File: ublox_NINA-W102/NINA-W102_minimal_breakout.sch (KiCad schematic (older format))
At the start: 15 parts, among them J1 Conn_01x15, J2 Conn_01x15, J3 6_PIN_SERIAL_TARGETLOCK, SW1 BOOT, SW2 RESET, U1 NINA-W102

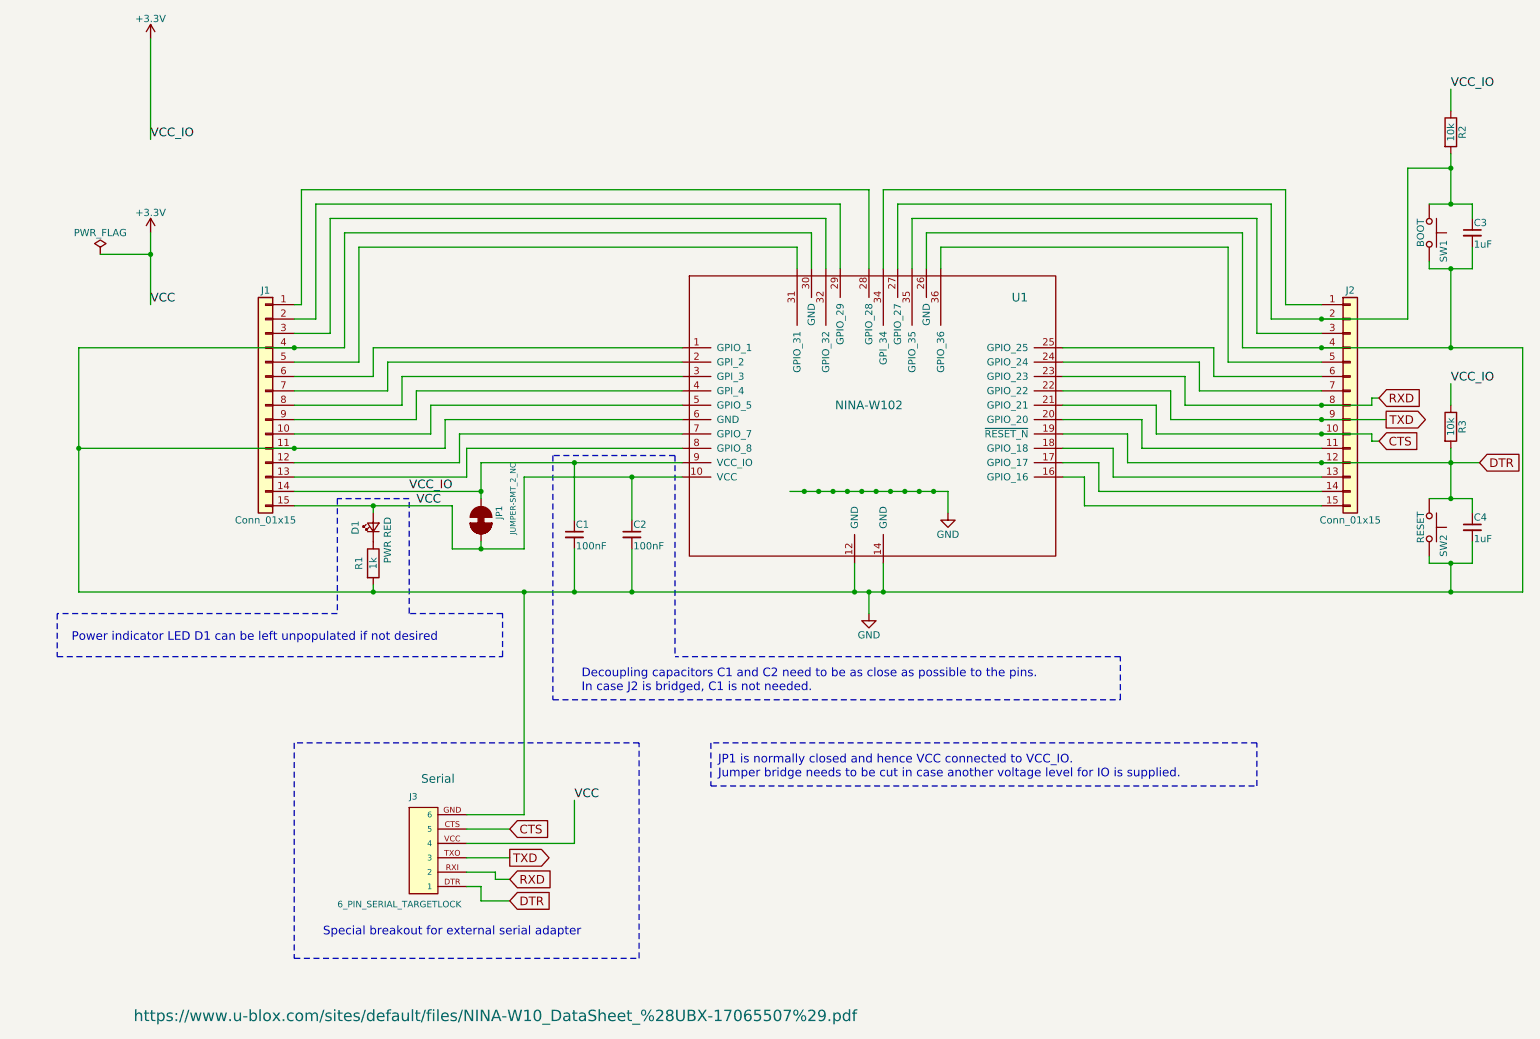
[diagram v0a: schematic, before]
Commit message: Fixed CTS PIN and added fpx sample mage from sensirion
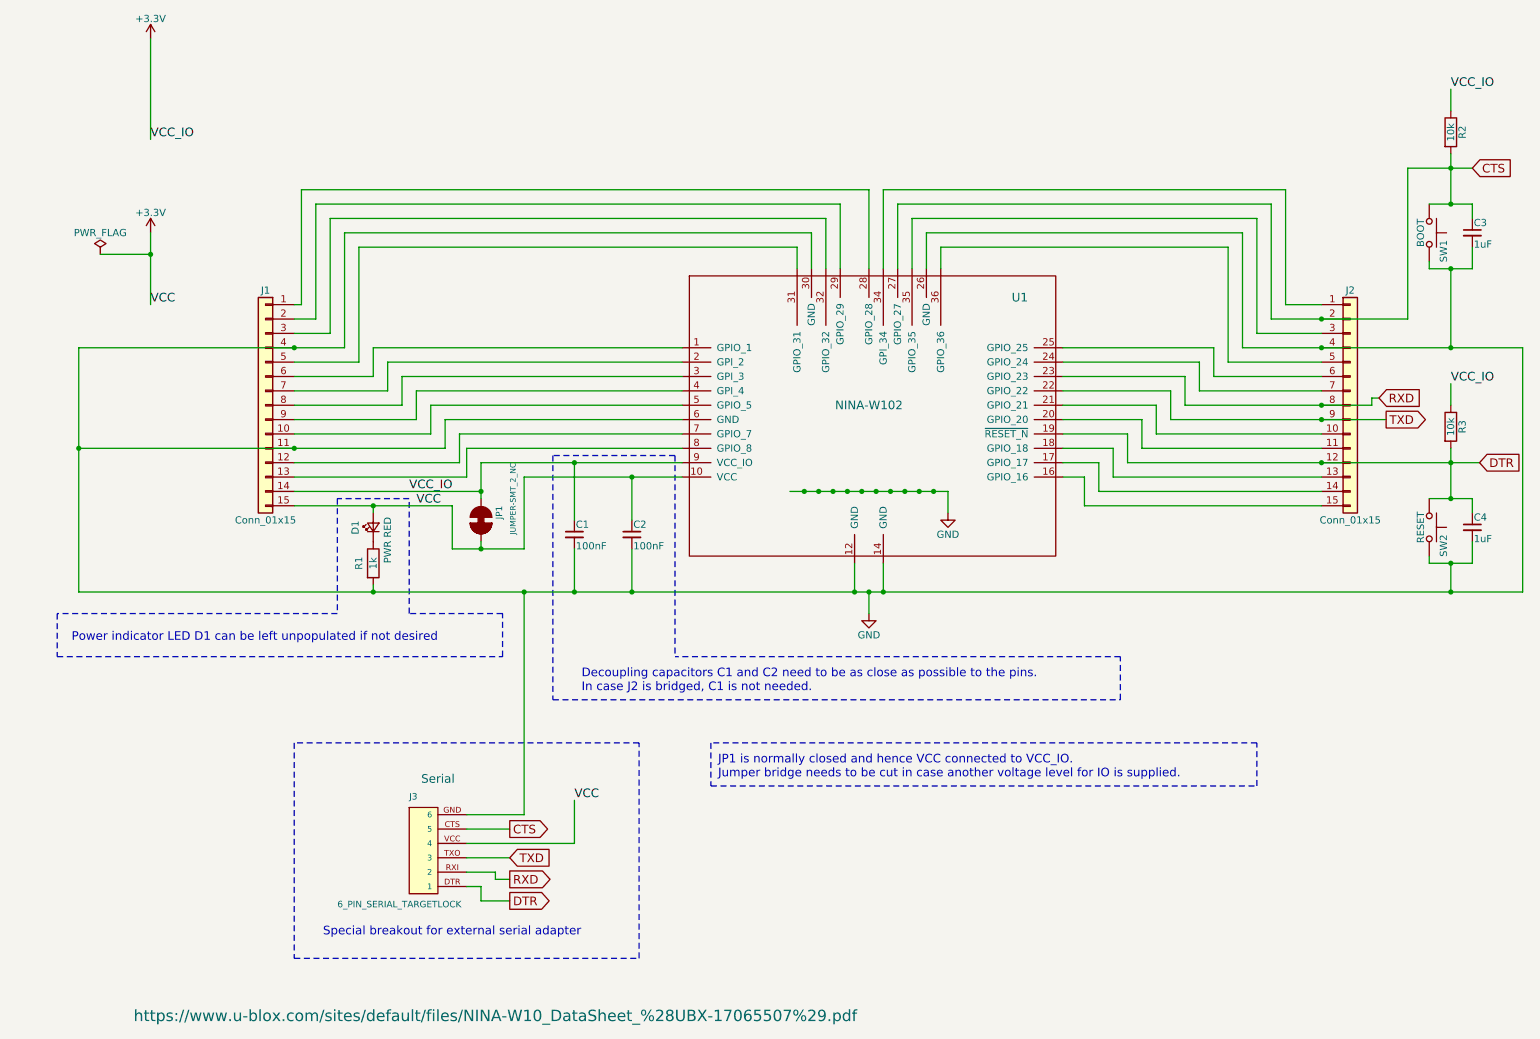
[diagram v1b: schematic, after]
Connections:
- net CTS: now also C3.1, J2.2 (Pin_2), R2.2, SW1.1, U1.27 (GPIO_27); no longer J2.10 (Pin_10), U1.21 (GPIO_21)
- new net: J2.10 (Pin_10), U1.21 (GPIO_21)
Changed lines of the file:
@@
 Sheet 1 1
 Title "ublox NINA-W102 minimal breakout"
-Date "2018-04-17"
-Rev "0.3"
+Date "2018-04-18"
+Rev "0.4"
 Comp "GDG Zürich"
 Comment1 "Michel Racic"
@@
 Text GLabel 9950 3300 2    60   Input ~ 0
 RXD
-Text GLabel 3900 6650 2    60   Input ~ 0
+Text GLabel 3900 6650 2    60   Output ~ 0
 RXD
-Text GLabel 3900 6500 2    60   Output ~ 0
+Text GLabel 3900 6500 2    60   Input ~ 0
 TXD
-Text GLabel 3900 6800 2    60   Input ~ 0
+Text GLabel 3900 6800 2    60   Output ~ 0
 DTR
-Text GLabel 3900 6300 2    60   Input ~ 0
+Text GLabel 3900 6300 2    60   Output ~ 0
 CTS
 Text GLabel 10650 3750 2    60   Input ~ 0
@@
 Text GLabel 10000 3450 2    60   Output ~ 0
 TXD
-Text GLabel 9950 3600 2    60   Input ~ 0
+Text GLabel 10600 1700 2    60   Input ~ 0
 CTS
 Text Notes 2600 7050 0    60   ~ 0
@@
 Wire Wire Line
 	8300 3450 7750 3450
-Wire Wire Line
-	8400 3550 9900 3550
 Wire Wire Line
 	8400 3550 8400 3350
@@
 	10150 2750 10150 1700
 Wire Wire Line
-	10150 1700 10450 1700
+	10150 1700 10600 1700
 Connection ~ 9550 2750
 Wire Wire Line
@@
 Connection ~ 9550 3350
 Connection ~ 9550 3450
-Connection ~ 9550 3550
 Wire Notes Line
 	2400 5700 2400 7200
@@
 Wire Wire Line
 	9900 3300 9900 3350
-Wire Wire Line
-	9950 3600 9900 3600
-Wire Wire Line
-	9900 3600 9900 3550
 Wire Wire Line
 	3700 4300 3700 4350
@@
 	1    0    0    -1
 $EndComp
+Wire Wire Line
+	2400 4050 3500 4050
+Text Label 10450 3200 0    60   ~ 0
+VCC_IO
+Text Label 3200 3950 0    60   ~ 0
+VCC_IO
+Wire Wire Line
+	8200 3750 10650 3750
+Wire Wire Line
+	2400 3950 3700 3950
+Text Label 3250 4050 0    60   ~ 0
+VCC
+Wire Wire Line
+	1400 2300 1050 2300
+Text Label 1400 2650 0    60   ~ 0
+VCC
+Text Label 10450 1150 0    60   ~ 0
+VCC_IO
+Text Label 4350 6100 0    60   ~ 0
+VCC
+Connection ~ 2400 2950
+Wire Wire Line
+	9550 3550 8400 3550
+Text Label 1400 1500 0    60   ~ 0
+VCC_IO
+Wire Wire Line
+	1400 800  1400 1500
 $Comp
 L +3.3V #PWR_IO05
@@
 	1    0    0    -1
 $EndComp
-Wire Wire Line
-	1400 800  1400 1500
-Wire Wire Line
-	2400 4050 3500 4050
-Text Label 10450 3200 0    60   ~ 0
-VCC_IO
-Text Label 3200 3950 0    60   ~ 0
-VCC_IO
-Text Label 1400 1500 0    60   ~ 0
-VCC_IO
-Wire Wire Line
-	8200 3750 10650 3750
-Wire Wire Line
-	2400 3950 3700 3950
-Text Label 3250 4050 0    60   ~ 0
-VCC
-Wire Wire Line
-	1400 2300 1050 2300
-Text Label 1400 2650 0    60   ~ 0
-VCC
-Text Label 10450 1150 0    60   ~ 0
-VCC_IO
-Text Label 4350 6100 0    60   ~ 0
-VCC
-Connection ~ 2400 2950
 $EndSCHEMATC

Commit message: initial layout done without wiring
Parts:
- J3: footprint Connectors-SparkFun:1X06_LOCK -> Connectors-SparkFun:6_PIN_SERIAL_TARGET_SIDE_W_SILK; symbol 6_PIN_SERIAL_TARGETLOCK -> 6_PIN_SERIAL_TARGETSILK
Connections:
- net +3V3: no longer C1.1, J1.14 (Pin_14), JP1.1, R2.1, R3.1, U1.9 (VCC_IO)
- new net +1V8: C1.1, J1.14 (Pin_14), JP1.1, R2.1, R3.1, U1.9 (VCC_IO)
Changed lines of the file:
@@
 Power indicator LED D1 can be left unpopulated if not desired
 $Comp
-L 6_PIN_SERIAL_TARGETLOCK J3
+L 6_PIN_SERIAL_TARGETSILK J3
 U 1 1 5AD510E3
 P 3400 6700
 F 0 "J3" H 3200 7300 45  0000 L BNN
 F 1 "6_PIN_SERIAL_TARGETLOCK" H 2700 6550 45  0000 L BNN
-F 2 "Connectors-SparkFun:1X06_LOCK" H 3400 7400 20  0001 C CNN
+F 2 "Connectors-SparkFun:6_PIN_SERIAL_TARGET_SIDE_W_SILK" H 3400 7400 20  0001 C CNN
 F 3 "" H 3400 6700 50  0001 C CNN
 F 4 "Serial" H 3400 7450 60  0000 C CNN "Field4"
@@
 	1400 800  1400 1500
 $Comp
-L +3.3V #PWR_IO05
+L +1V8 #PWR_IO05
 U 1 1 5AD5EE0C
 P 1400 800
 F 0 "#PWR_IO05" H 1400 650 50  0001 C CNN
-F 1 "+3.3V" H 1400 940 50  0000 C CNN
+F 1 "+1V8" H 1400 940 50  0000 C CNN
 F 2 "" H 1400 800 50  0001 C CNN
 F 3 "" H 1400 800 50  0001 C CNN

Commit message: Added printouts and BOM
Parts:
- J3: Assembly (none) -> Left unpopulated
- JP1: Assembly (none) -> Nothing to assemble
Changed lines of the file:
@@
 F 3 "" H 3400 6700 50  0001 C CNN
 F 4 "Serial" H 3400 7450 60  0000 C CNN "Field4"
+F 5 "Left unpopulated" H 3400 6700 60  0001 C CNN "Assembly"
 	1    3400 6700
 	1    0    0    -1
@@
 F 2 "Jumpers:SMT-JUMPER_2_NC_TRACE_SILK" H 3700 4350 20  0001 C CNN
 F 3 "" H 3700 4150 60  0001 C CNN
+F 4 "Nothing to assemble" H 3700 4150 60  0001 C CNN "Assembly"
 	1    3700 4150
 	0    1    1    0

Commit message: Added schematic components to local library
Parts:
- J3: footprint Connectors-SparkFun:6_PIN_SERIAL_TARGET_SIDE_W_SILK -> lib:6_PIN_SERIAL_TARGET_SIDE_W_SILK
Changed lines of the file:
@@
 LIBS:dk_Trimmer-Potentiometers
 LIBS:dk_USB-DVI-HDMI-Connectors
+LIBS:components
 LIBS:NINA-W102_minimal_breakout-cache
 EELAYER 25 0
@@
 F 0 "J3" H 3200 7300 45  0000 L BNN
 F 1 "6_PIN_SERIAL_TARGETLOCK" H 2700 6550 45  0000 L BNN
-F 2 "Connectors-SparkFun:6_PIN_SERIAL_TARGET_SIDE_W_SILK" H 3400 7400 20  0001 C CNN
+F 2 "lib:6_PIN_SERIAL_TARGET_SIDE_W_SILK" H 3400 7400 20  0001 C CNN
 F 3 "" H 3400 6700 50  0001 C CNN
 F 4 "Serial" H 3400 7450 60  0000 C CNN "Field4"
